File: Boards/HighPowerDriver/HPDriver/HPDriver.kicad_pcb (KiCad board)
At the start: 4 copper layers, 100.6 x 76.2 mm, 150 parts, among them J1 60V_In, J2 USB_B_Mini, J3 Coils, J4 Control, J5 AVR-UPDI-6, Q1 IRFR5410, Q10 IRF4950S, Q11 BC817, Q12 BC817, Q13 BC817, Q14 BC817, Q2 IRFR3910, Q3 IRFR3910, Q4 IRFR5410, Q5 IRFR5410, Q6 IRFR3910, Q7 IRFR3910, Q8 IRFR5410, Q9 BC817, SW1 SW_Push, U1 LM5009MM, U10 74LVC1G123, U11 ATtiny406-S, U12 74AHC1G00, U13 74LVC1G125, U14 74LVC1G125, U2 TMC262, U3 FT230XS, U4 SFH6156, U5 SFH6156, U6 TLP118, U7 LTV-827S, U8 LTV-827S, U9 74HC14, X1 16MHz

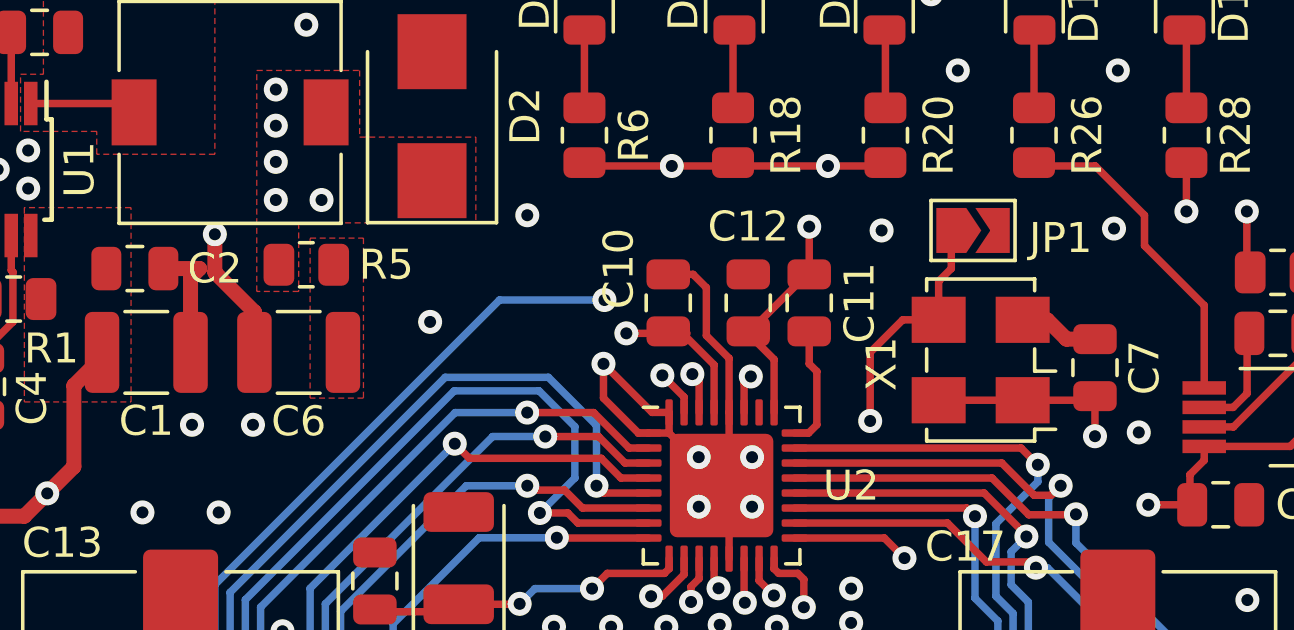
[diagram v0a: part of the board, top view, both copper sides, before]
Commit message: Minor Layout fix
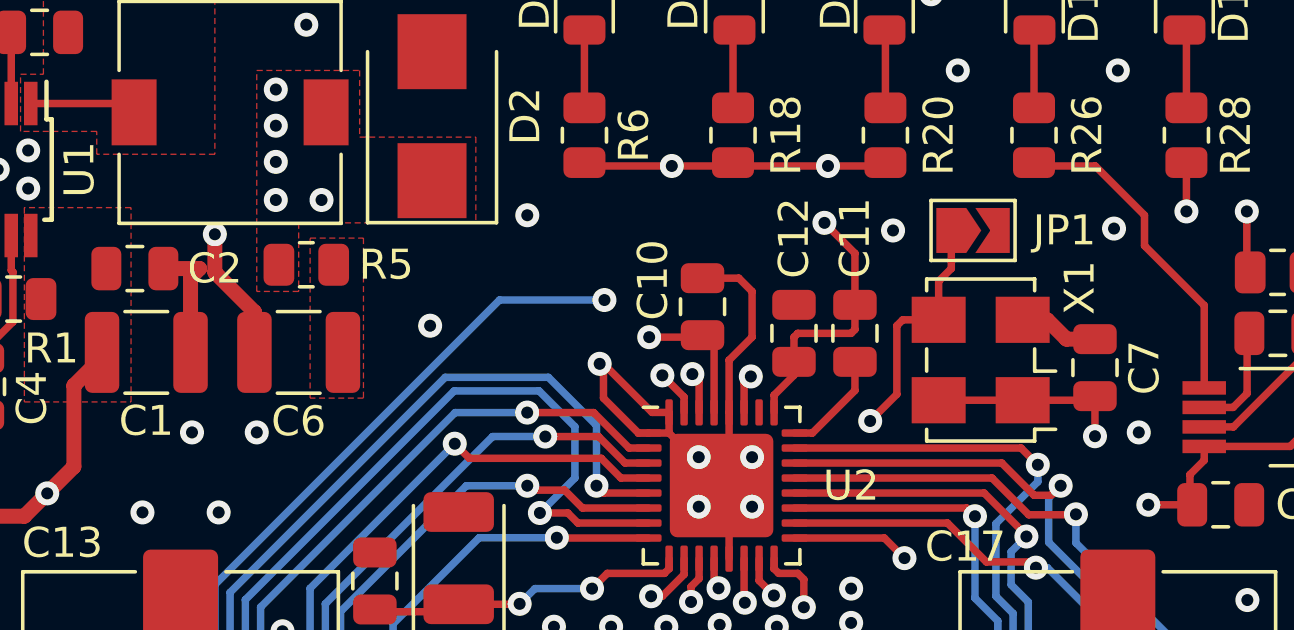
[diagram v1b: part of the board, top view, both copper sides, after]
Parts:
- moved C11 1.83 mm to (126.0, 82.8)
- moved C12 1.83 mm to (124.0, 82.8)
- moved C10 1.15 mm to (120.9, 81.9)
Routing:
- net +48V: track 90.2 -> 92.0 mm
- net Net-(C11-Pad2): track 4.07 -> 3.55 mm

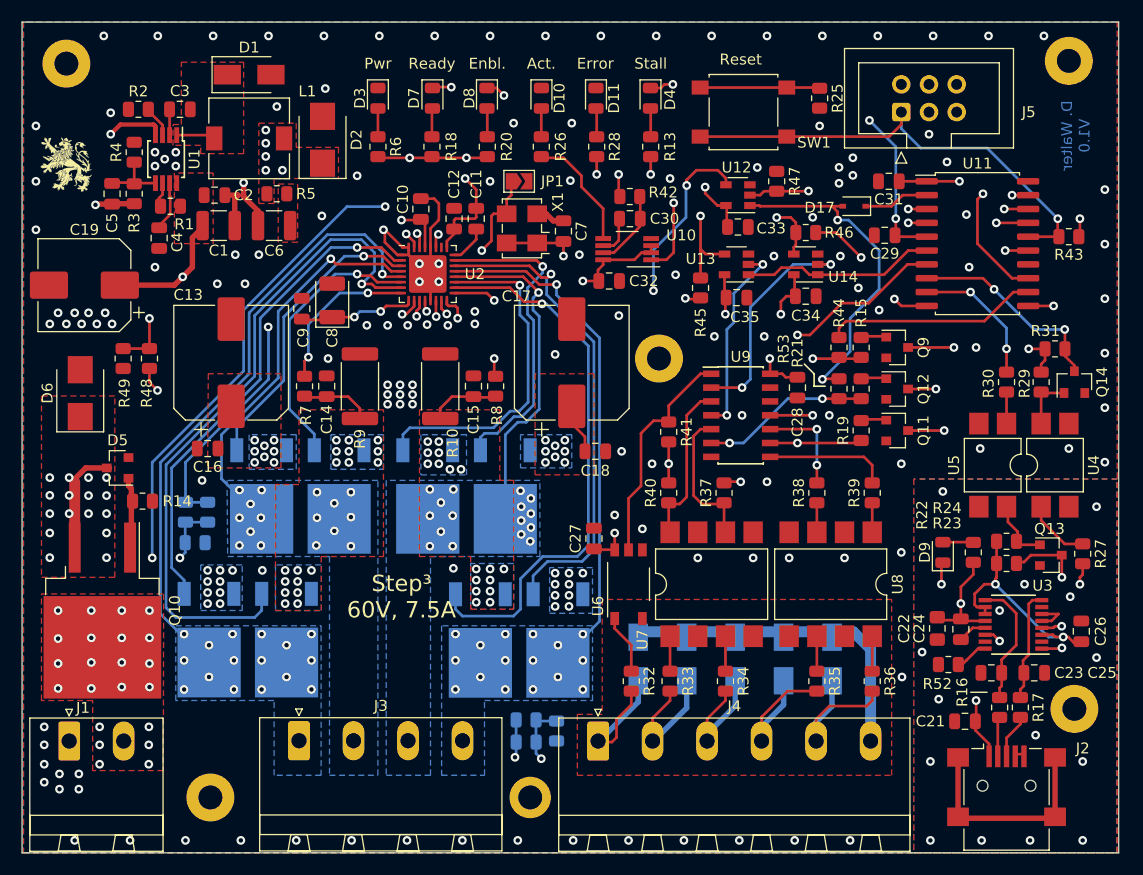
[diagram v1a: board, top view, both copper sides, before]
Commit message: Changed Controller to ATmega328PB
The ATtiny did not have enough flash
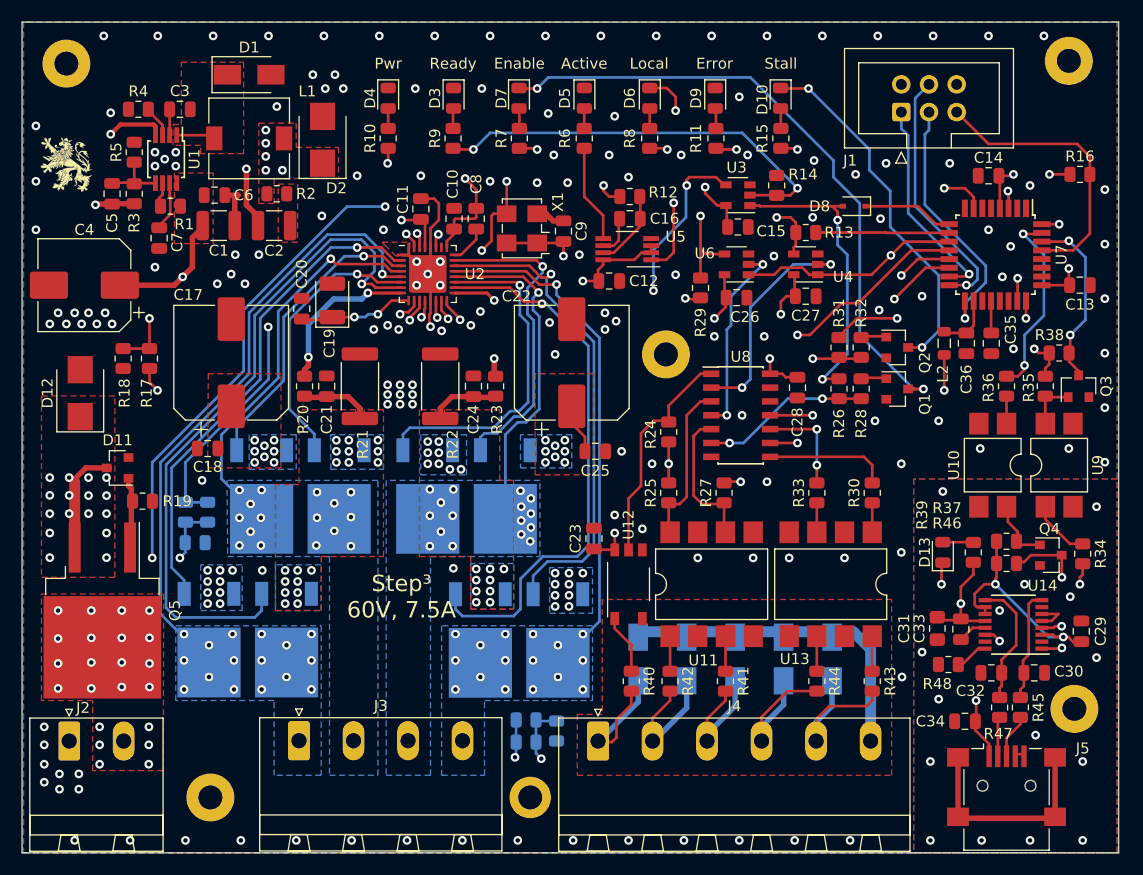
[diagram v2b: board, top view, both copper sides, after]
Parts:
- removed JP1: Clk_En, Jumper:SolderJumper-2_P1.3mm_Open_TrianglePad1.0x1.5mm
- removed the Q11 at (164.6, 102.2)
- removed the R19 at (161.3, 102.2)
- removed the R25 at (157.5, 71.8)
- removed SW1: SW_Push, Button_Switch_SMD:SW_SPST_B3S-1000
- added C35: 100nF, Capacitor_SMD:C_0805_2012Metric, F.Cu at (173.2, 94.2)
- added C36: 100nF, Capacitor_SMD:C_0805_2012Metric, F.Cu at (170.9, 94.2)
- added D6: LED_Ye, LED_SMD:LED_0805_2012Metric, F.Cu at (141.9, 71.8)
- added L2: 10µH, Inductor_SMD:L_0805_2012Metric, F.Cu at (168.9, 94.2)
- added R8: 180R, Resistor_SMD:R_0805_2012Metric, F.Cu at (141.9, 75.4)
- J1: renamed from J5; value AVR-UPDI-6 -> AVR-ISP-6
- U7: renamed from U11; value ATtiny406-S -> ATmega328PB-A; footprint Package_SO:SOIC-20W_7.5x12.8mm_P1.27mm -> Package_QFP:TQFP-32_7x7mm_P0.8mm
- moved C13 18.5 mm to (181.4, 88.9), turned to 0 degrees
- moved R15 12.0 mm to (153.9, 75.4)
- moved D10 11.9 mm to (153.9, 71.8)
- moved R11 11.0 mm to (148.0, 75.4)
- moved D9 10.9 mm to (147.9, 71.8)
- moved C14 9.16 mm to (173.0, 78.9)
- moved R16 5.80 mm to (181.4, 78.7), turned to 0 degrees
- moved R6 4.01 mm to (135.9, 75.4)
- moved D5 3.94 mm to (135.9, 71.8)
- moved R7 3.04 mm to (129.9, 75.4)
- moved D7 2.94 mm to (129.9, 71.8)
- moved R9 2.08 mm to (123.9, 75.4)
- moved U7 1.94 mm to (173.6, 86.1), turned to -90 degrees
- moved D3 1.94 mm to (123.9, 71.8)
- moved R10 1.21 mm to (117.9, 75.4)
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- renumbered C12 to C10, C10 to C11, C32 to C12, C29 to C13, C31 to C14, C33 to C15, C30 to C16, C13 to C17, C16 to C18, C8 to C19, C6 to C2, C9 to C20, C14 to C21, C17 to C22, C27 to C23, C15 to C24, C18 to C25, C35 to C26, C34 to C27, C26 to C29, C25 to C30, C22 to C31, C23 to C32, C24 to C33, C21 to C34, C19 to C4, C2 to C6, C4 to C7, C11 to C8, C7 to C9, D4 to D10, D5 to D11, D6 to D12, D9 to D13, D15 to D14, D12 to D15, D13 to D16, D16 to D17, D14 to D18, D7 to D3, D3 to D4, D10 to D5, D8 to D7, D17 to D8, D11 to D9, J1 to J2, J2 to J5, Q12 to Q1, Q3 to Q10, Q4 to Q11, Q5 to Q12, Q6 to Q13, Q9 to Q2, Q14 to Q3, Q13 to Q4, Q10 to Q5, Q7 to Q6, Q8 to Q7, Q1 to Q8, Q2 to Q9, R6 to R10, R28 to R11, R42 to R12, R46 to R13, R47 to R14, R13 to R15, R43 to R16, R48 to R17, R49 to R18, R14 to R19, R5 to R2, R7 to R20, R9 to R21, R10 to R22, R8 to R23, R41 to R24, R40 to R25, R53 to R26, R37 to R27, R21 to R28, R45 to R29, R39 to R30, R44 to R31, R15 to R32, R38 to R33, R27 to R34, R29 to R35, R30 to R36, R24 to R37, R31 to R38, R22 to R39, R2 to R4, R32 to R40, R34 to R41, R33 to R42, R36 to R43, R35 to R44, R17 to R45, R23 to R46, R16 to R47, R52 to R48, R12 to R49, R4 to R5, R11 to R51, R51 to R52, R26 to R6, R20 to R7, R18 to R9, TH2 to TH1, TH1 to TH2, U5 to U10, U7 to U11, U6 to U12, U8 to U13, U3 to U14, U12 to U3, U14 to U4, U10 to U5, U13 to U6, U9 to U8, U4 to U9
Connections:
- D3 pad 1: Net-(D7-Pad1) (its old number) -> GND
- J1 pad 1: /Connector/Reset -> /Controller/MOSI
- J1 pad 3: unconnected-(J5-Pad3) -> /Controller/SCK
- J1 pad 4: unconnected-(J5-Pad4) -> /Controller/MISO
- J1 pad 5: unconnected-(J5-Pad5) -> /Controller/Reset
- R14 pad 2: /Controller/Ready_Ctrler -> /Controller/Ready_Ctrlr
- R16 pad 2: /Connector/Reset -> /Controller/Reset
- R31 pad 2: Net-(R44-Pad2) -> Net-(R31-Pad2)
- R9 pad 1: +5V -> /Controller/Ready_Ctrlr
- U2 pad 16: Net-(JP1-Pad1) -> /Controller/Clk
- U3 pad 2: /Controller/Ready_Ctrler -> /Controller/Ready_Ctrlr
- U7 pad 1: +5V -> unconnected-(U7-Pad1)
- U7 pad 10: /Controller/Dir_Local -> /Controller/Step_Local
- U7 pad 11: /Controller/Step_Local -> /Controller/Local_Ctrl
- U7 pad 12: Net-(R44-Pad2) -> /Controller/Ready_Ctrlr
- U7 pad 13: /Connector/Error -> /Controller/CS_TMC
- U7 pad 14: unconnected-(U11-Pad14) -> /Controller/Dir_Local
- U7 pad 15: /Controller/CS_TMC -> /Controller/MOSI
- U7 pad 16: /Connector/Reset -> /Controller/MISO
- U7 pad 17: /Controller/MOSI -> /Controller/SCK
- U7 pad 18: /Controller/MISO -> Net-(C36-Pad1)
- U7 pad 19: /Controller/SCK -> unconnected-(U7-Pad19)
- U7 pad 2: /Controller/Enable_Ctrlr -> unconnected-(U7-Pad2)
- U7 pad 20: GND -> Net-(C35-Pad1)
- U7 pad 3: /Controller/Temp1 -> /Connector/Error
- U7 pad 4: /Controller/Temp2 -> +5V
- U7 pad 5: /Connector/VSup -> GND
- U7 pad 6: /Controller/Local_Ctrl -> unconnected-(U7-Pad6)
- U7 pad 7: /Controller/Ready_Ctrler -> /Controller/Clk
- U7 pad 8: /Connector/Rx -> unconnected-(U7-Pad8)
- U7 pad 9: /Connector/Tx -> /Controller/Enable_Ctrlr
- U8 pad 9: /Controller/Ready_Ctrler -> /Controller/Ready_Ctrlr
- X1 pad 3: Net-(JP1-Pad1) -> /Controller/Clk
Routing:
- net /Controller/Ready_Ctrlr: track 0.00 -> 81.8 mm, vias 0 -> 4
- net Net-(D7-Pad1) (its old number): track 76.4 -> 0.00 mm, vias 3 -> 0
- net /Controller/Clk: track 0.00 -> 63.1 mm, vias 0 -> 4
- net /Controller/Ready_Ctrler: track 51.8 -> 0.00 mm, vias 3 -> 0
- net /Connector/Reset: track 43.7 -> 0.00 mm, vias 1 -> 0
- net Net-(R31-Pad2): track 0.00 -> 35.6 mm, vias 0 -> 2
- net /Controller/Local_Ctrl: track 17.8 -> 53.1 mm, vias 0 -> 2
- net /Controller/Reset: track 0.00 -> 26.0 mm
- net /Connector/VSup: track 112.3 -> 135.4 mm, vias 3 -> 2
- net Net-(R44-Pad2): track 19.5 -> 0.00 mm
- net /Controller/SCK: track 65.9 -> 85.2 mm
- net /Controller/MISO: track 66.6 -> 85.7 mm
- net /Connector/Error: track 49.8 -> 31.3 mm
- net Net-(JP1-Pad1): track 17.7 -> 0.00 mm, vias 2 -> 0
- net Net-(D10-Pad1): track 50.5 -> 33.1 mm, vias 3 -> 2
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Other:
- board text added: "Active"
- board text added: "Enable"
- board text added: "Local"
- board text removed: "Act."
- board text removed: "Enbl."
- board text removed: "Reset"
